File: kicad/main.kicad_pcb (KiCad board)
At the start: 2 copper layers, 162.2 x 137.3 mm, 43 parts, among them J1 Barrel_Jack, P1 Mini-DIN_6pins_ver3, SW1 Reset, SW2 SW_DIP_x08, U1 KM1810VM88, U10 L7805, U11 15 MHz, U12 8255, U13 74HC273, U14 74HC244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

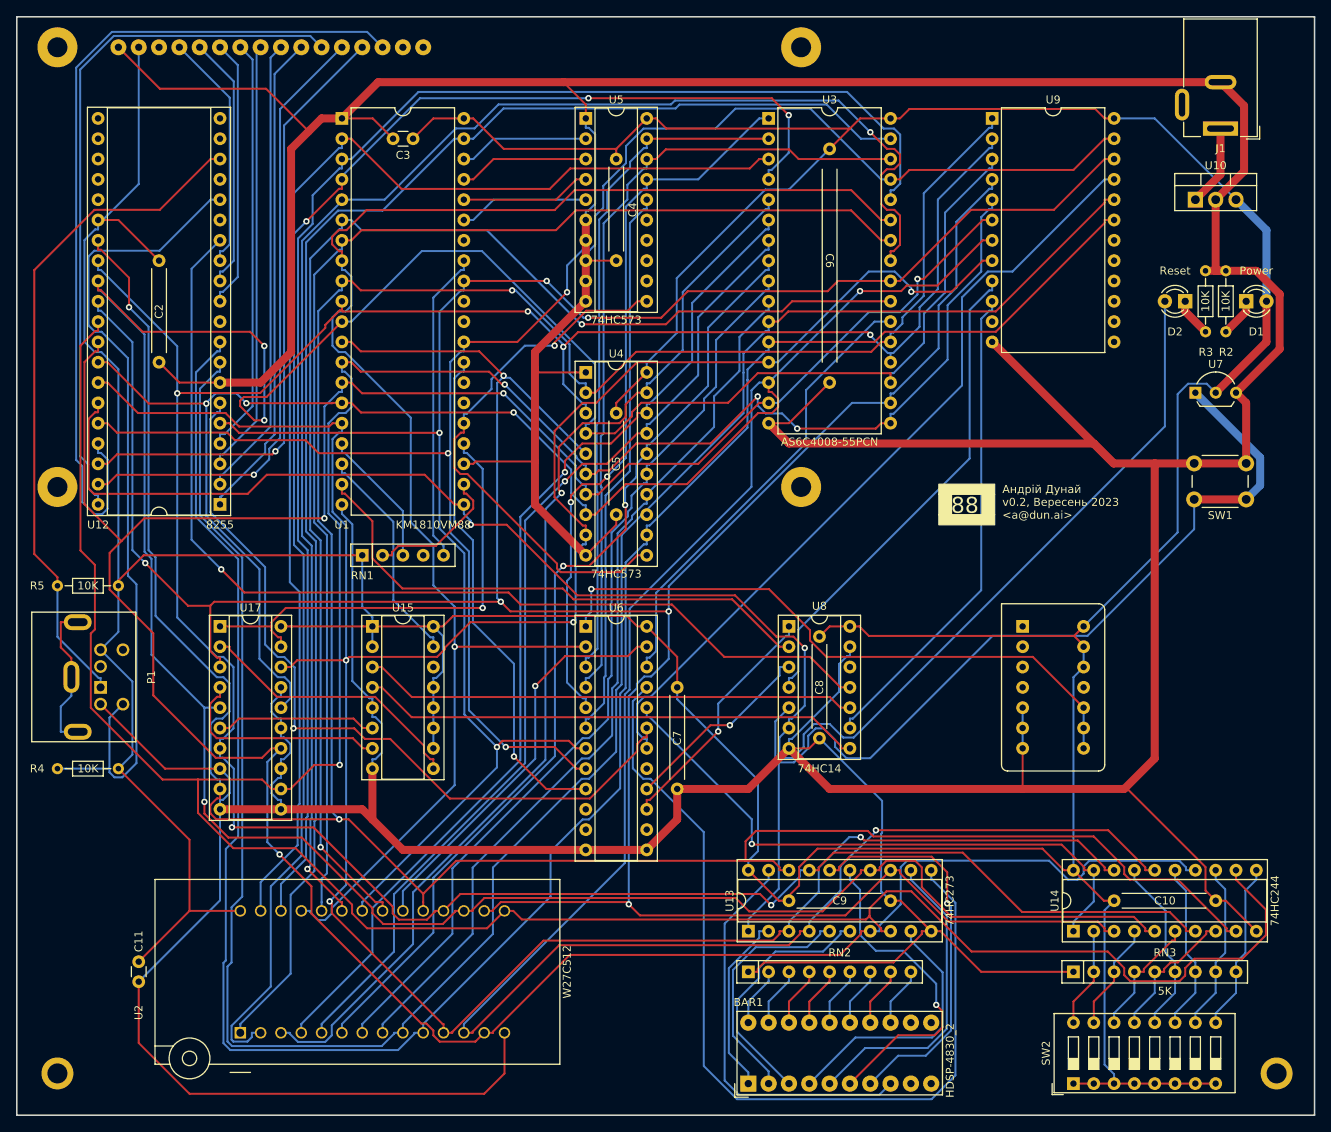
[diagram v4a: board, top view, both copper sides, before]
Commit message: Add UART & uSD card
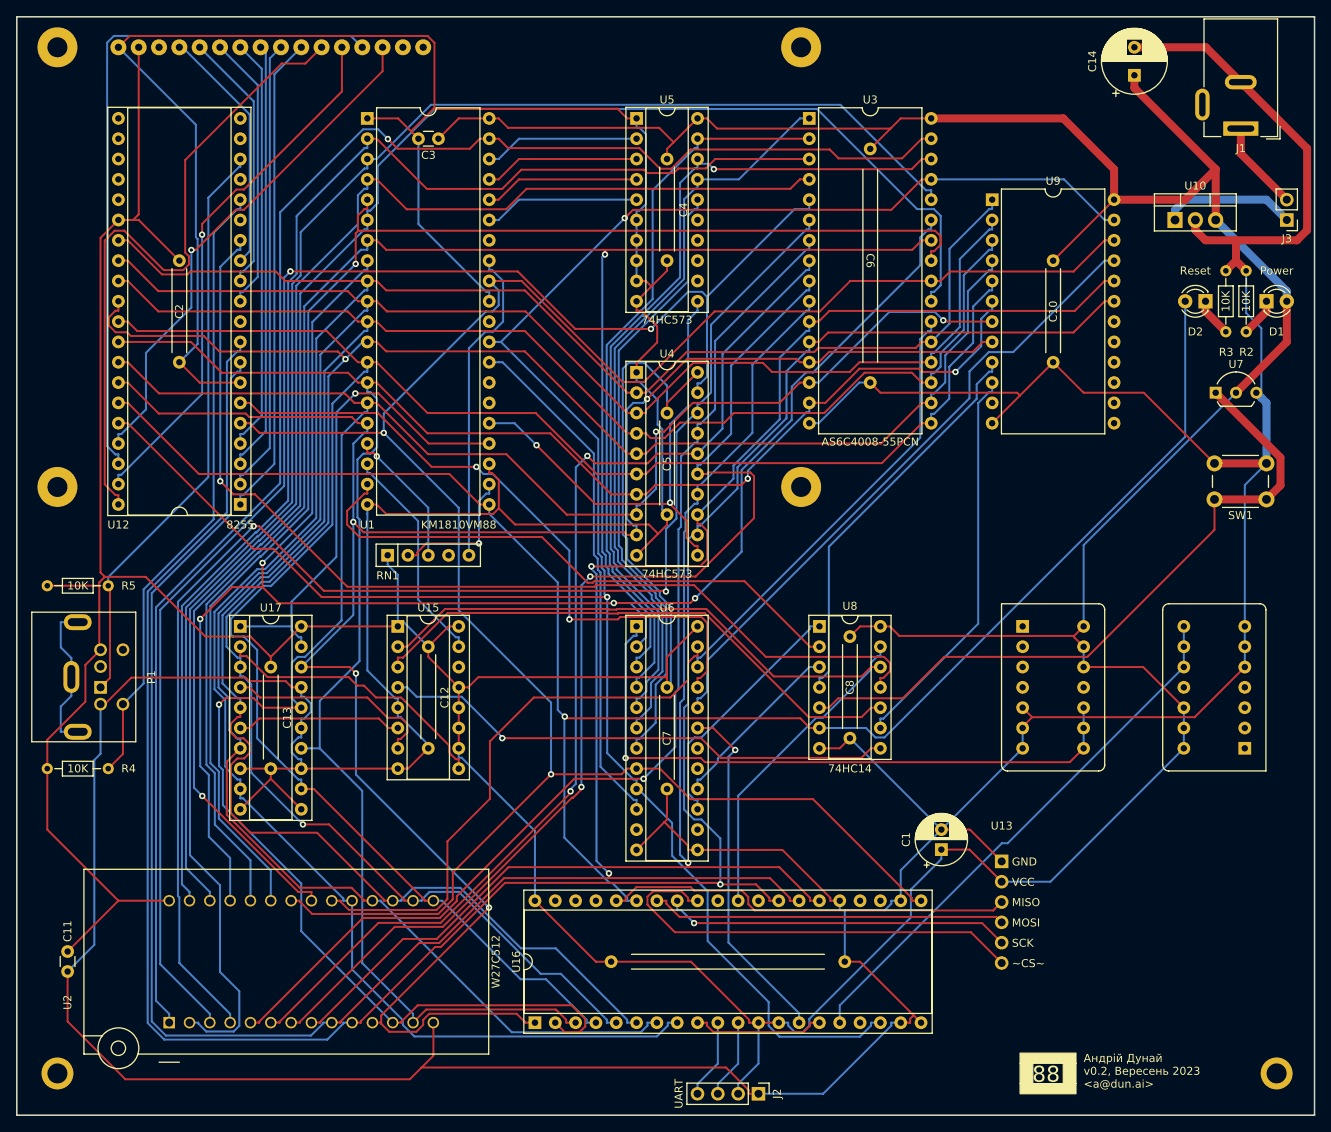
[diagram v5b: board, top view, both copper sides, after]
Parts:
- removed BAR1: HDSP-4830_2, Display:HDSP-4830
- removed RN2: 330R, Resistor_THT:R_Array_SIP9
- removed RN3: 5K, Resistor_THT:R_Array_SIP9
- removed SW2: SW_DIP_x08, Button_Switch_THT:SW_DIP_SPSTx08_Slide_9.78x22.5mm_W7.62mm_P2.54mm
- removed U14: 74HC244, Package_DIP:DIP-20_W7.62mm_Socket
- added C1: 10 uF, Capacitor_THT:CP_Radial_D6.3mm_P2.50mm, F.Cu at (130.8, -5.12)
- added C12: 0.1 uF, footprints:C_Disc_Long, F.Cu at (66.7, -30.5)
- added C13: 0.1 uF, footprints:C_Disc_Long, F.Cu at (47.0, -27.9)
- added C14: 10 uF, Capacitor_THT:CP_Radial_D8.0mm_P3.50mm, F.Cu at (154.9, -101.9)
- added J2: UART, Connector_PinHeader_2.54mm:PinHeader_1x04_P2.54mm_Vertical, F.Cu at (108.0, 25.4)
- added J3: ~, Connector_PinHeader_2.54mm:PinHeader_1x02_P2.54mm_Vertical, F.Cu at (174.0, -83.8)
- added U16: 16550, Package_DIP:DIP-40_W15.24mm_Socket, F.Cu at (80.0, 16.5)
- added U18: 1.8432 MHz, footprints:Oscillator_DIP-8-14, F.Cu at (165.1, -25.4)
- C9: footprint footprints:C_Disc_Long -> footprints:C_Disc_VeryLong
- U13: value 74HC273 -> uSD adapter; footprint Package_DIP:DIP-20_W7.62mm_Socket -> footprints:MicroSD-Adapter
- moved C10 80.4 mm to (144.8, -78.7), turned to -90 degrees
- moved U13 32.5 mm to (135.8, -9.36), turned to 0 degrees
- moved C9 17.6 mm to (95.9, 8.89)
- moved U9 10.2 mm to (137.2, -86.4)
- moved C11 8.98 mm to (21.6, 7.62)
- moved U2 8.98 mm to (34.3, 16.5)
- moved R4 8.89 mm to (19.1, -15.2), turned to 0 degrees
- moved R5 8.89 mm to (19.1, -38.1), turned to 0 degrees
- moved C4 6.35 mm to (96.5, -91.4)
- moved C5 6.35 mm to (96.5, -59.7)
- moved U4 6.35 mm to (92.7, -64.8)
- moved U5 6.35 mm to (92.7, -96.5)
- moved U6 6.35 mm to (92.7, -33.0)
- moved C6 5.08 mm to (121.9, -86.4)
- moved U3 5.08 mm to (114.3, -96.5)
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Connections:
- net Net-(U11-OUT) renamed MCLK
- J1 pad 1: Net-(U10-IN) -> Net-(J3-Pin_2)
- U10 pad 1: Net-(U10-IN) -> Net-(J3-Pin_1)
- U13 pad 1: ~{RES} -> GND
- U13 pad 2: Net-(U13-Q0) -> +5V
- U13 pad 3: AD_{0} -> Net-(U13-MISO)
- U13 pad 4: AD_{1} -> Net-(U13-MOSI)
- U15 pad 2: +5V -> ~{INT2}
- U6 pad 10: unconnected-(U6-I-Pad10) -> IO/~{M}
- U6 pad 18: TIMER~{EN} -> unconnected-(U6-I/O/Q-Pad18)
- U6 pad 19: IO~{EN} -> UART~{EN}
- U6 pad 20: IN~{EN} -> TIMER~{EN}
- U6 pad 21: OUT~{EN} -> IO~{EN}
- U6 pad 3: A_{16} -> A_{9}
- U6 pad 4: A_{17} -> A_{16}
- U6 pad 5: A_{18} -> A_{17}
- U6 pad 6: A_{19} -> A_{18}
- U6 pad 7: ~{RD} -> A_{19}
- U6 pad 8: ~{WR} -> ~{RD}
- U6 pad 9: IO/~{M} -> ~{WR}
- U8 pad 12: unconnected-(U8-Pad12) -> ~{INT2}
- U8 pad 13: GND -> Net-(U16-INTR)
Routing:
- net AD_{3}: track 424.7 -> 248.5 mm, vias 4 -> 0
- net AD_{7}: track 416.6 -> 281.9 mm, vias 3 -> 0
- net AD_{2}: track 375.4 -> 244.9 mm, vias 4 -> 2
- net AD_{5}: track 391.9 -> 272.8 mm, vias 3 -> 0
- net AD_{4}: track 376.2 -> 259.0 mm, vias 5 -> 2
- net AD_{1}: track 384.2 -> 267.3 mm, vias 5 -> 3
- net OUT~{EN}: track 113.6 -> 0.00 mm
- net AD_{0}: track 347.5 -> 255.3 mm, vias 5 -> 4
- net AD_{6}: track 357.9 -> 275.2 mm, vias 6 -> 0
- net IN~{EN}: track 75.7 -> 0.00 mm, vias 1 -> 0
- net UARTCLK: track 0.00 -> 67.8 mm
- net ~{INT2}: track 0.00 -> 66.3 mm
- net A_{9}: track 158.1 -> 220.9 mm, vias 0 -> 1
- net ~{RD}: track 221.4 -> 282.4 mm, vias 4 -> 2
- net ~{WR}: track 217.2 -> 274.0 mm, vias 3 -> 2
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
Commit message: Move chips to center/bottom
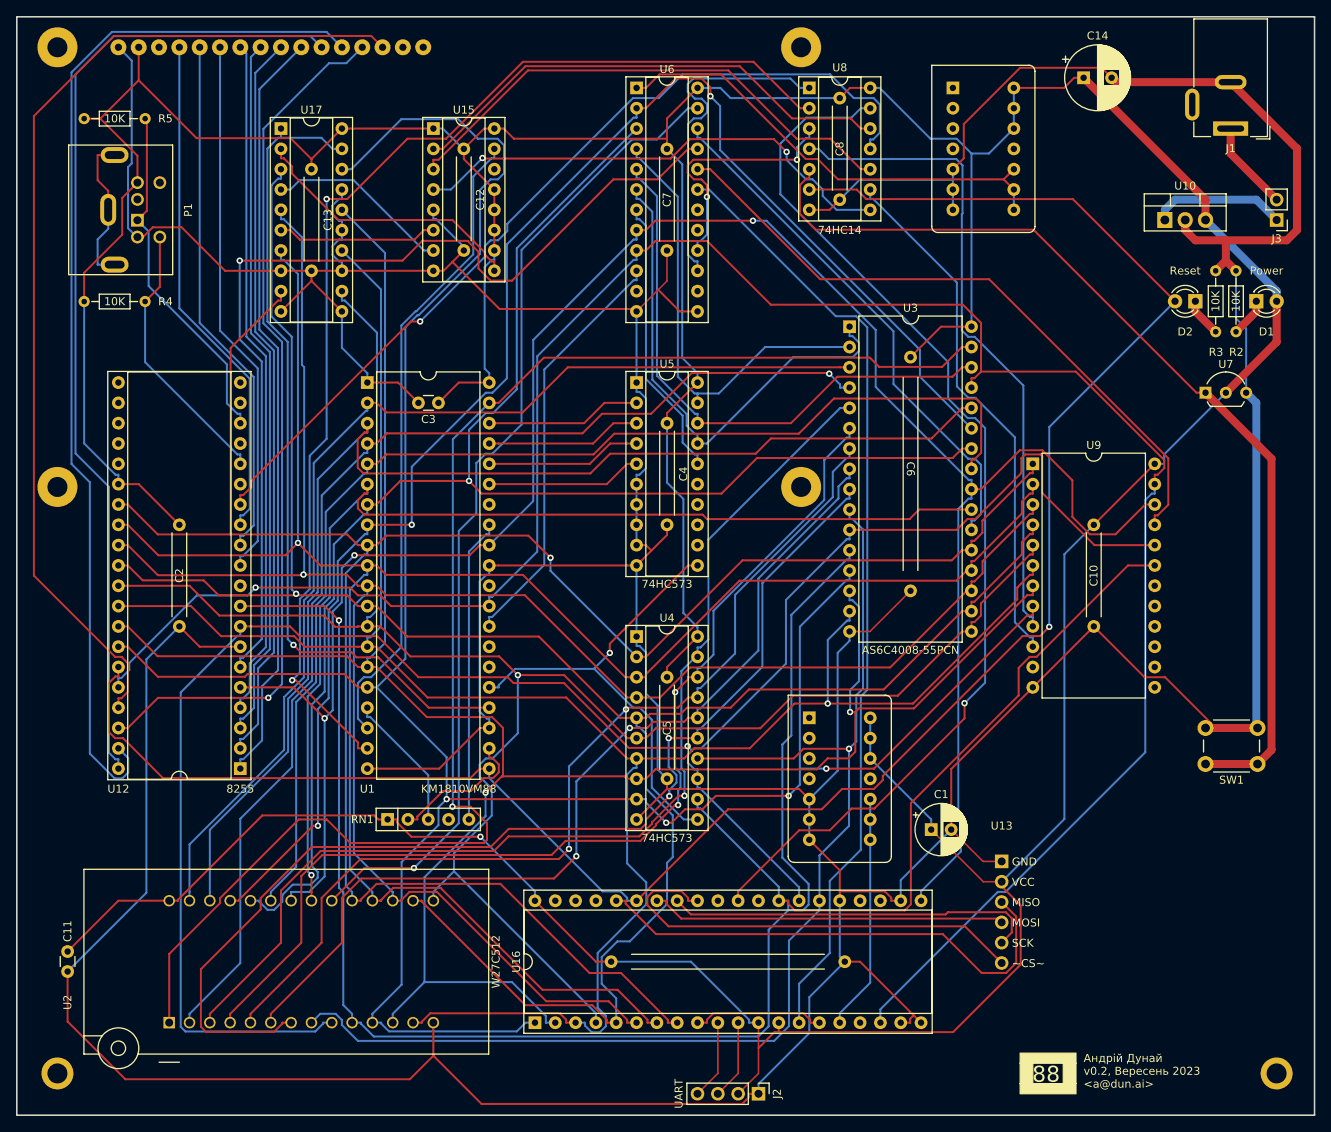
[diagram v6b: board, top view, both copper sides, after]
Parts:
- moved U11 67.9 mm to (135.9, -92.7)
- moved C8 67.3 mm to (118.1, -99.1)
- moved U8 67.3 mm to (114.3, -100.3)
- moved C7 67.3 mm to (96.5, -92.7)
- moved U6 67.3 mm to (92.7, -100.3)
- moved C13 62.4 mm to (52.1, -90.2)
- moved U17 62.4 mm to (48.3, -95.2)
- moved U15 62.4 mm to (67.3, -95.2)
- moved C12 62.4 mm to (71.1, -92.7)
- moved P1 58.6 mm to (30.3, -83.8)
- moved R4 58.6 mm to (23.7, -73.6)
- moved R5 58.6 mm to (23.7, -96.5)
- moved U18 48.5 mm to (117.9, -14.0), turned to -90 degrees
- moved C10 33.4 mm to (149.9, -45.7)
- moved U9 33.4 mm to (142.2, -53.3)
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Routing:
- net Net-(U16-INTR): track 39.8 -> 135.6 mm, vias 0 -> 1
- net UART~{EN}: track 44.0 -> 118.8 mm, vias 1 -> 0
- net CLK: track 71.8 -> 145.1 mm, vias 0 -> 2
- net GND: track 888.4 -> 821.4 mm
- net Net-(LCD1-D_{5}): track 66.9 -> 132.7 mm, vias 1 -> 0
- net AD_{0}: track 255.3 -> 319.9 mm
- net Net-(LCD1-D_{7}): track 64.3 -> 128.3 mm, vias 1 -> 0
- net A_{10}: track 199.1 -> 137.0 mm
- net A_{1}: track 309.9 -> 248.2 mm, vias 2 -> 1
- net A_{7}: track 191.7 -> 134.1 mm, vias 2 -> 1
- net ROM~{EN}: track 70.3 -> 124.6 mm, vias 0 -> 1
- net INTR: track 28.0 -> 80.7 mm
- net +5V: track 730.6 -> 680.9 mm, vias 0 -> 1
- net A_{6}: track 178.1 -> 130.5 mm
- net PS2CLK: track 78.2 -> 34.3 mm
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
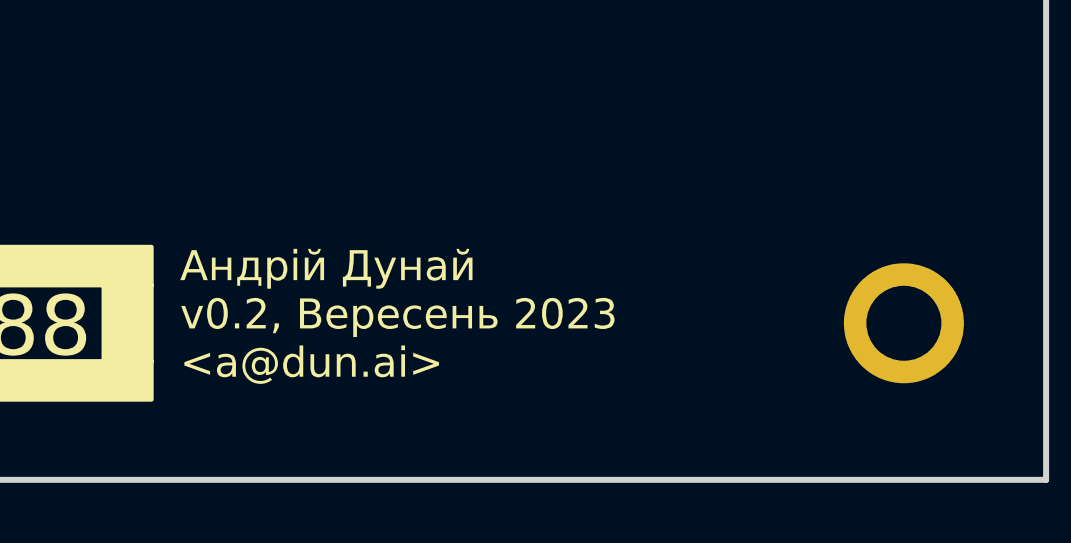
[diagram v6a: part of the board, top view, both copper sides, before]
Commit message: Update PCB label
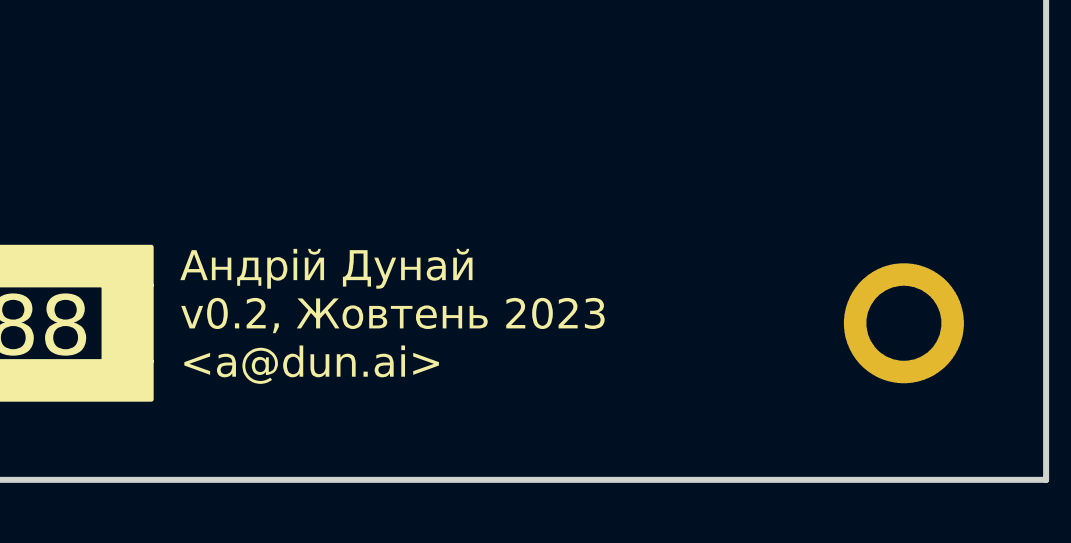
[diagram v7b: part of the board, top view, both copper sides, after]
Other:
- board text added: "Андрій Дунай v0.2, Жовтень 2023 <a@dun.ai>"
- board text removed: "Андрій Дунай v0.2, Вересень 2023 <a@dun.ai>"
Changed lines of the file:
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@@
   (gr_rect (start 15.24 -109.22) (end 177.46 28.08)
     (stroke (width 0.2) (type default)) (fill none) (layer "Edge.Cuts"))
-  (gr_text "Андрій Дунай\nv0.2, Вересень 2023\n<a@dun.ai>" (at 148.59 24.765) (layer "F.SilkS")
+  (gr_text "Андрій Дунай\nv0.2, Жовтень 2023\n<a@dun.ai>" (at 148.59 24.765) (layer "F.SilkS")
     (effects (font (size 1 1) (thickness 0.15)) (justify left bottom))
   )

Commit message: Add 8259 interrupt controller, update PCB
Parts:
- removed C13: 0.1 uF, footprints:C_Disc_Long
- removed U15: 74HC148, Package_DIP:DIP-16_W7.62mm_Socket
- removed U17: 74HC244, Package_DIP:DIP-20_W7.62mm_Socket
- added U14: 8259, Package_DIP:DIP-28_W15.24mm_Socket, F.Cu at (34.3, 76.2)
- C12: footprint footprints:C_Disc_Long -> footprints:C_Disc_VeryLong
- moved C12 180.2 mm to (41.9, 85.1)
- moved R5 147.3 mm to (23.6, 50.8)
- moved P1 146.6 mm to (30.2, 62.8)
- moved R4 144.8 mm to (23.6, 71.1)
- moved RN1 128.5 mm to (68.6, 119.4)
- moved U13 128.4 mm to (174.6, 113.0), turned to -90 degrees
- moved U18 127.8 mm to (131.9, 113.0)
- moved J2 127.6 mm to (120.7, 152.4)
- moved C9 127.6 mm to (108.6, 135.9)
- moved U16 127.6 mm to (92.7, 143.5)
- moved H1 127.1 mm to (25.4, 149.9)
- moved H2 127.1 mm to (177.8, 149.9)
- moved C11 127.1 mm to (26.7, 134.6)
- moved C14 127.1 mm to (153.7, 25.4)
- moved C6 127.1 mm to (132.0, 66.7)
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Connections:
- U12 pad 14: Net-(U12-PC0) -> INT1
- U16 pad 30: Net-(U16-INTR) -> INT4
- U6 pad 18: unconnected-(U6-I/O/Q-Pad18) -> INT~{EN}
- U8 pad 10: ~{INT1} -> unconnected-(U8-Pad10)
- U8 pad 11: Net-(U12-PC0) -> unconnected-(U8-Pad11)
- U8 pad 12: ~{INT2} -> unconnected-(U8-Pad12)
- U8 pad 13: Net-(U16-INTR) -> unconnected-(U8-Pad13)
- U8 pad 8: ~{INT0} -> unconnected-(U8-Pad8)
- U8 pad 9: Net-(U9-OUT0) -> unconnected-(U8-Pad9)
- U9 pad 10: Net-(U9-OUT0) -> INT0
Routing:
- net Net-(U16-INTR): track 135.6 -> 0.00 mm, vias 1 -> 0
- net ~{RD}: track 273.7 -> 400.7 mm, vias 3 -> 2
- net Net-(U12-PC0): track 112.5 -> 0.00 mm, vias 1 -> 0
- net INT0: track 0.00 -> 112.1 mm
- net Net-(LCD1-D_{7}): track 128.3 -> 27.3 mm
- net INT4: track 0.00 -> 94.6 mm, vias 0 -> 1
- net Net-(LCD1-D_{5}): track 132.7 -> 38.6 mm
- net INT~{EN}: track 0.00 -> 93.7 mm
- net Net-(LCD1-D_{4}): track 122.5 -> 43.4 mm
- net IO~{EN}: track 121.6 -> 43.0 mm, vias 1 -> 0
- net Net-(LCD1-D_{6}): track 109.7 -> 33.1 mm, vias 1 -> 0
- net INT1: track 0.00 -> 74.9 mm
- net Net-(U9-OUT0): track 66.5 -> 0.00 mm
- net Net-(LCD1-D_{3}): track 95.5 -> 29.3 mm
- net ~{INT1}: track 65.5 -> 0.00 mm
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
